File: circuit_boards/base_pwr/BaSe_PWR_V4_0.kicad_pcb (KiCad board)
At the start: 4 copper layers, 114.2 x 101.5 mm, 105 parts, among them J1 12VDC In, J10 Conn_01x04_Socket, J11 MOTOR, J12 USB3_A, J3 USB_B_Micro, J4 Conn_01x07_Pin, J5 Conn_02x06_Odd_Even, J6 USB3_B_Micro, J7 Conn_02x06_Odd_Even, J8 USB_C_Receptacle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

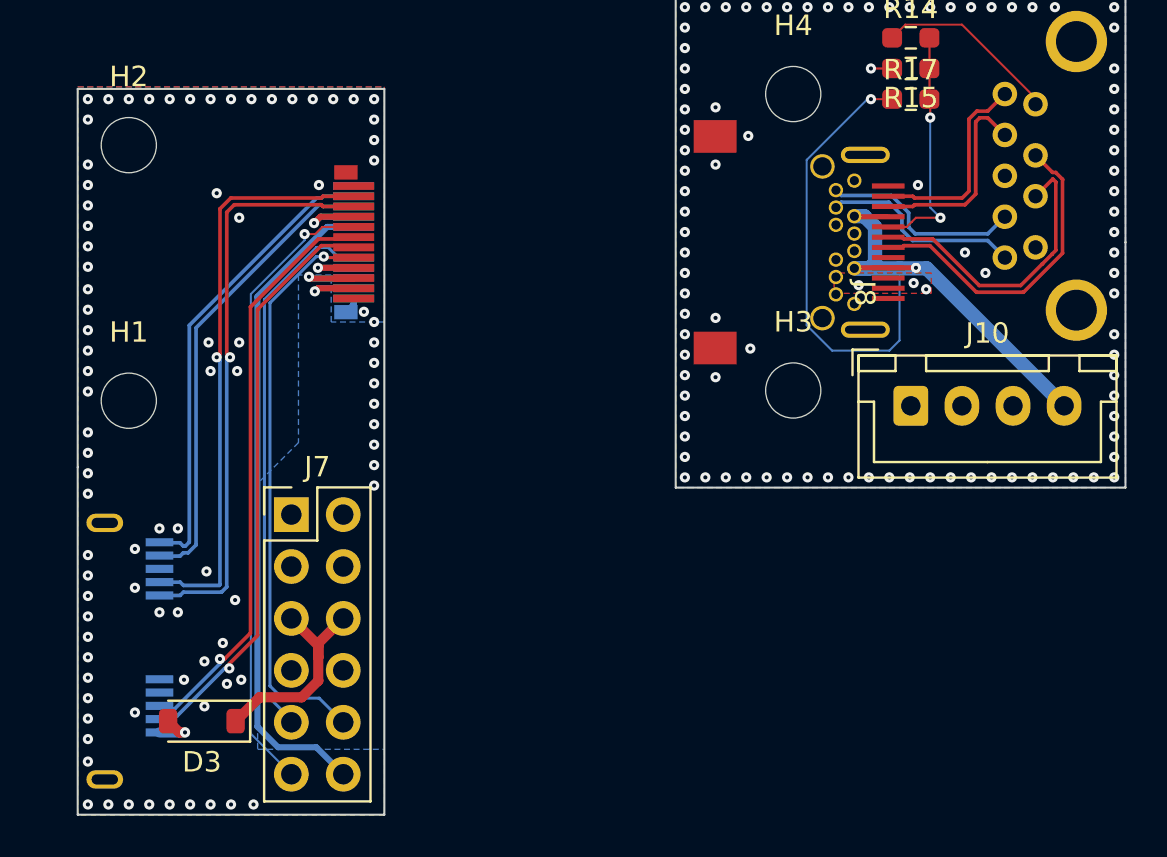
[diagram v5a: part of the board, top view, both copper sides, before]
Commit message: BaSe PWR V4.0: increase distance between USB lines and GND on same layers
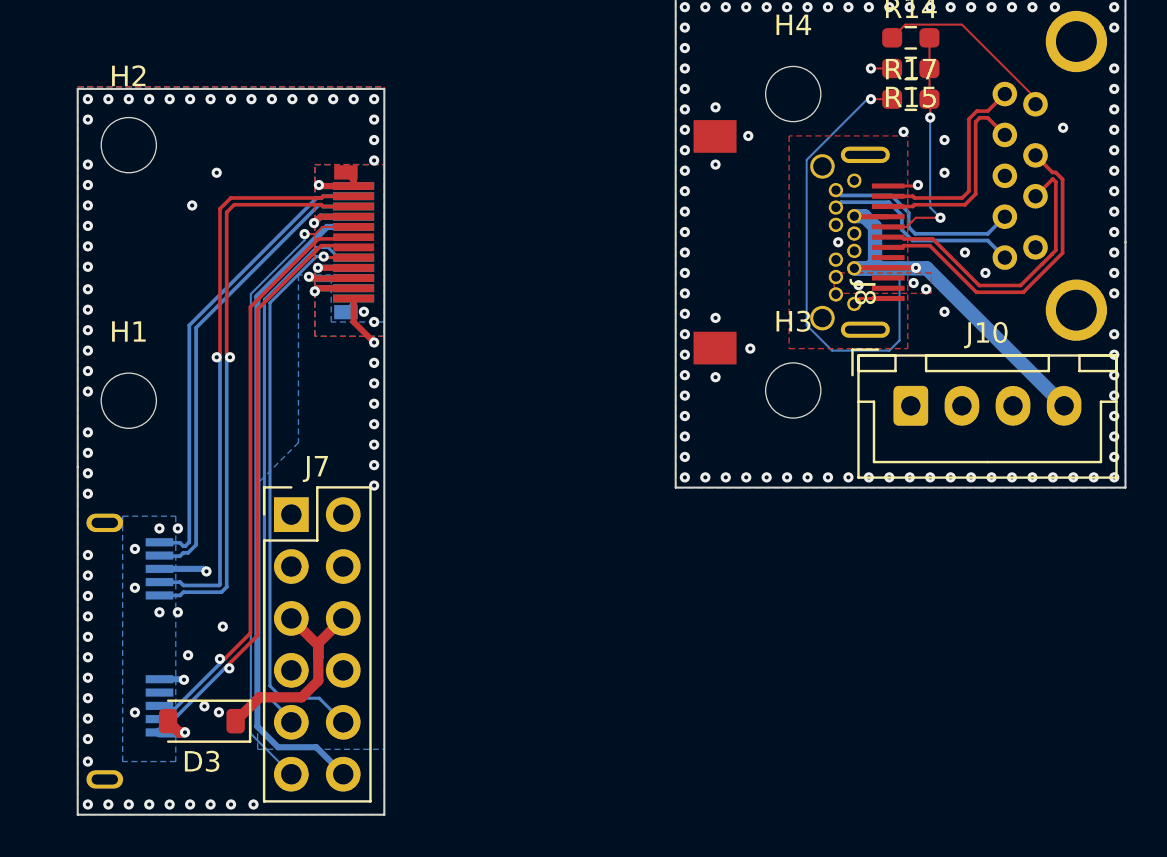
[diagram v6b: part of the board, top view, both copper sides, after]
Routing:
- net GND1: track 0.83 -> 11.2 mm, vias 87 -> 81
- net GND2: track 1.04 -> 4.28 mm, vias 94 -> 100
